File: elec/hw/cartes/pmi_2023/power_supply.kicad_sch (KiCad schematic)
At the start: 46 parts, among them J5 254, J8 254, Q3 DMP2008UFG-7, SW8 MSS12C02LS-BB2.0, U28 TLV61070A, U29 TLV61070A, U33 TLV61070A, U34 TLV61070A, U35 LDL1117S33R

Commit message: added oled display power supply res selectors, jlcpcb refs : wip
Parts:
- C27, C30, C39, C40: value 10µF 16V -> 10µF 25V; symbol cocotter_capacitors:C_10µF_16V_0805 -> cocotter_capacitors:C_10µF_25V_0805_X5R; JLCPCB (none) -> C15850; Specification 10µF 16V X7R 0805 -> 10µF 25V X7R 0805
- C29, C37, C41, C42: JLCPCB (none) -> C107079
- C46: symbol cocotter_capacitors:C_10µF_16V_0805_X5R -> cocotter_capacitors:C_10µF_25V_0805_X5R; Specification 10µF 25V X5R 0805 -> 10µF 25V X7R 0805
- D7: value red, 0603 -> white, 0603
- L1, L2, L3, L4: MOUSER (none) -> 581-LMLP07A7M2R2DTAS
- Q3: JLCPCB (none) -> C461052
- R107, R108, R111, R113: value 10k -> 10k 1%
- R110, R112, R67: value 90k -> 91k 1%; symbol cocotter_resistors:R_90k_0603_1% -> cocotter_resistors:R_91k_0603_1%; JLCPCB (none) -> C23265; Specification 90k 0603 1% 100mW -> 91k 0603 1% 100mW
- R66: JLCPCB (none) -> C23231
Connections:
- net GND: now also D7.1 (K); no longer D7.C
- net enable_pw_conv_3v7: now also D7.2 (A); no longer D7.A
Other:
- moved on the sheet: BT1

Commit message: reset button added to esp32 reset. uart prog connector replaces ftdi one
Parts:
- removed BT1: Battery_Cell, symbol Device:Battery_Cell
- added BT1: Battery 18650, symbol cocotter_others:Battery_Cell-18650
- D7: footprint cocotter_diodes:LED_0603_1608Metric -> (none)
- J5, J8: footprint cocotter_connectors:MY-18650-02 -> (none)

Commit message: pmi2023 : drc cleanup
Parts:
- D7: footprint (none) -> cocotter_diodes:LED_0603_1608Metric
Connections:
- net GND: now also D7.C; no longer D7.1 (C)
- net enable_pw_conv_3v7: now also D7.A; no longer D7.2 (A)
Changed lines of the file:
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@@
 			)
 		)
-		(property "Footprint" ""
+		(property "Footprint" "cocotter_diodes:LED_0603_1608Metric"
 			(at 82.55 62.23 0)
 			(effects
@@
 			)
 		)
-		(pin "1"
+		(pin "C"
 		)
-		(pin "2"
+		(pin "A"
 		)
 		(instances

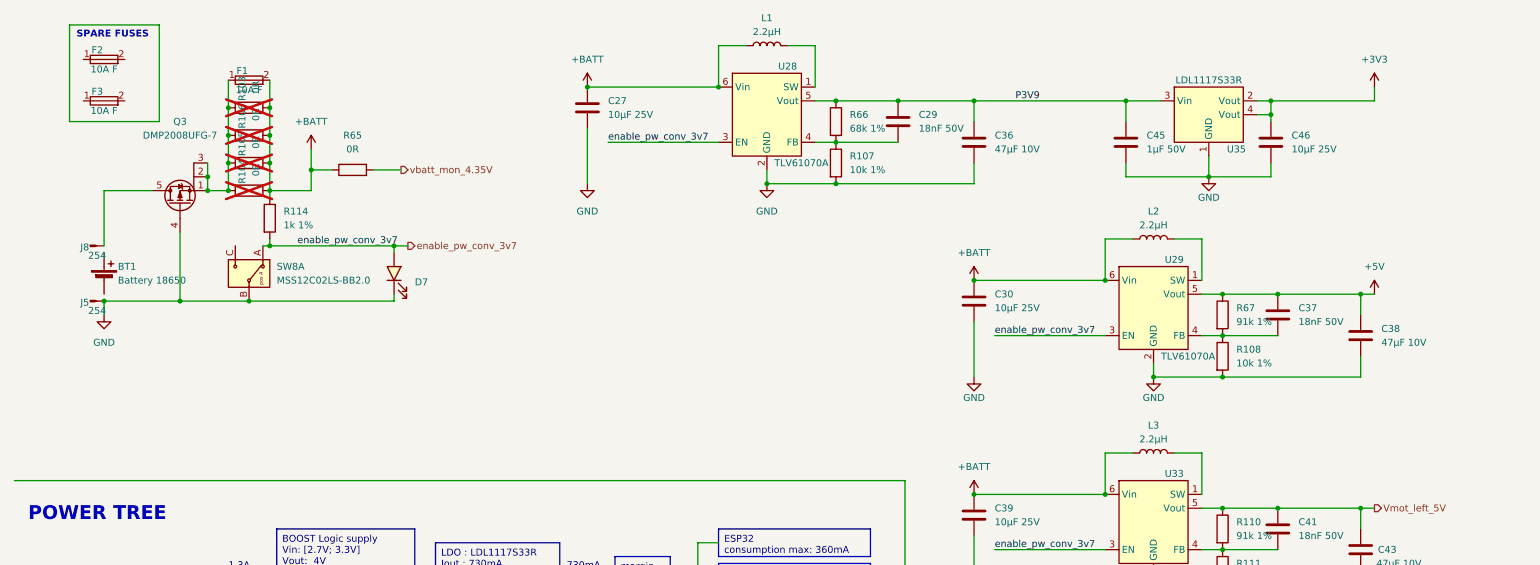
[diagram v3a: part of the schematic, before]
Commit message: routing cleanup, test points added to allow charging of battery in the pmi
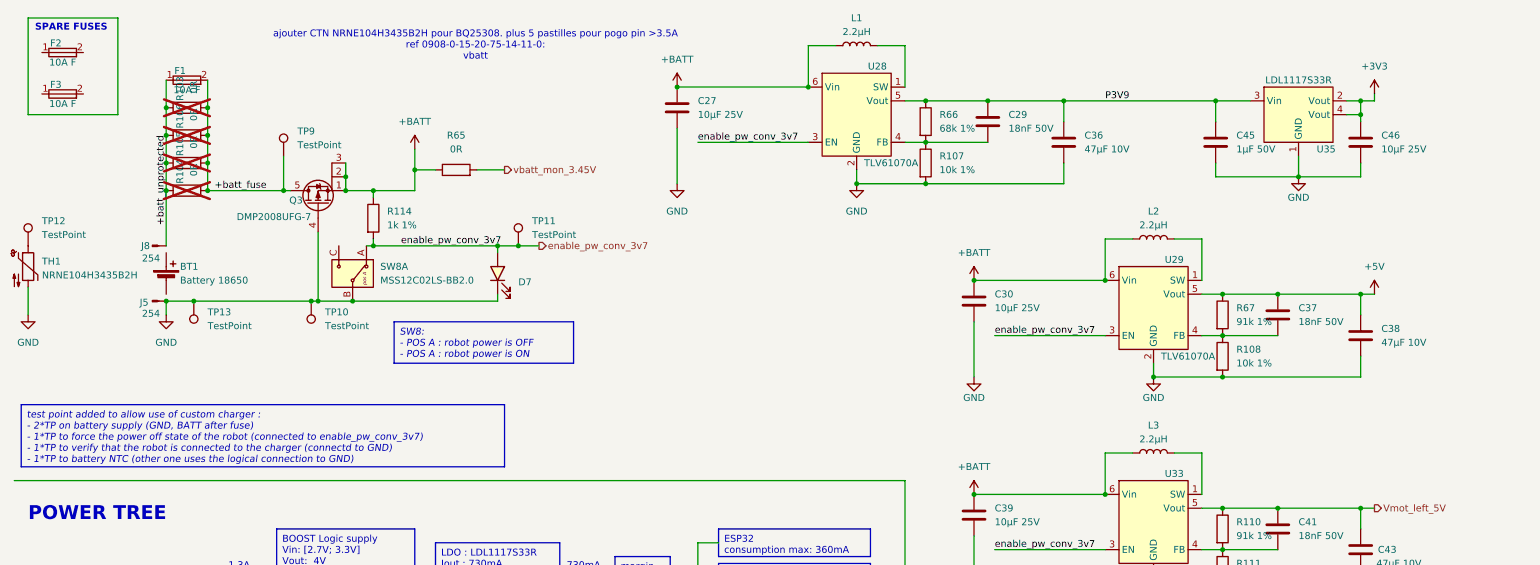
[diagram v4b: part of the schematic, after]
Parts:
- added TH1: NRNE104H3435B2H, cocotter_resistor:CTN-NRN, symbol cocotter_resistors:NRNE104H3435B2H
- added TP10, TP11, TP12, TP13, TP9: TestPoint, cocotter_others:testpoint-THT-0.5mm, symbol cocotter_others:TestPoint_for_pogo_pin-1mm
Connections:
- net +BATT: now also Q3.1 (S), Q3.2 (S), Q3.3 (S); no longer F1.2, R103.2, R104.2, R105.2, R106.2
- net GND: now also TH1.2, TP10.1, TP13.1
- net enable_pw_conv_3v7: now also TP11.1
- net +batt_unprotected: now reaches F1.1, R103.1, R104.1, R105.1, R106.1
- net +batt_unprotected: now also J8.1 (GND); no longer Q3.1 (S), Q3.2 (S), Q3.3 (S)
- net +batt_fuse: now reaches Q3.5 (D)
- net +batt_fuse: now also F1.2, R103.2, R104.2, R105.2, R106.2, TP9.1; no longer J8.1 (GND)
- net vbatt_mon_4.35V renamed vbatt_mon_3.45V
- new net: TH1.1, TP12.1
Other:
- note added: "ajouter CTN NRNE104H3435B2H pour BQ25308. plus 5 pastilles pour pogo pin >3.5A ref 0908-0-15-20-75-14-11-0: vbatt"
- moved on the sheet: BT1, C27, C29, C36, C45, C46, D7, F1, F2, F3, J5, J8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

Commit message: small changes
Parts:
- J5, J8: footprint (none) -> cocotter_connectors:254
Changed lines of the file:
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@@
 			)
 		)
-		(property "Footprint" ""
+		(property "Footprint" "cocotter_connectors:254"
 			(at 38.1 69.85 0)
 			(effects
@@
 			)
 		)
-		(property "Footprint" ""
+		(property "Footprint" "cocotter_connectors:254"
 			(at 38.1 59.69 0)
 			(effects

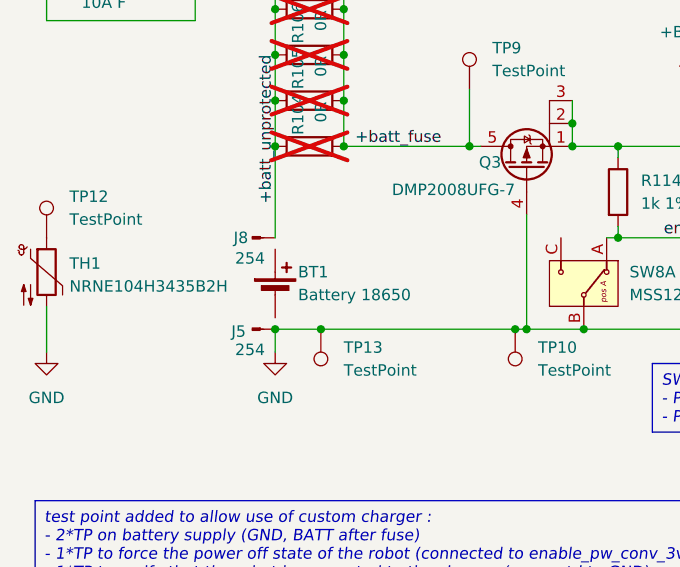
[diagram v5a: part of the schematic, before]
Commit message: PAMI 2023: update jlc part number
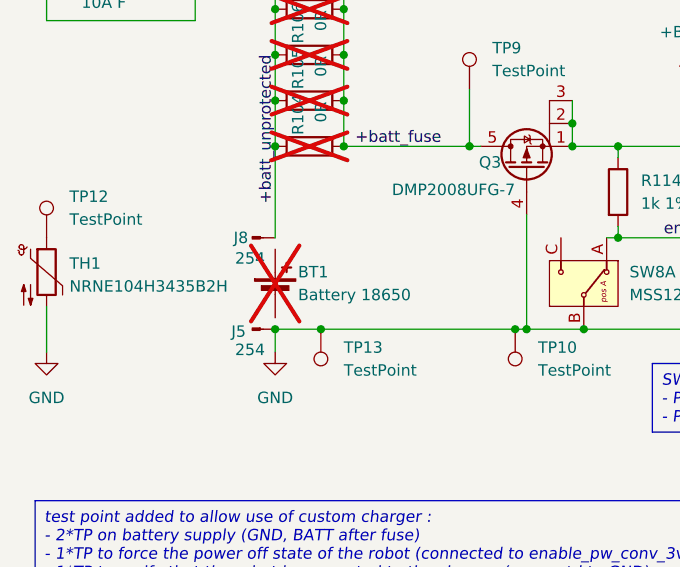
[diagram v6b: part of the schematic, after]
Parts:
- BT1: now not fitted
- L1, L2, L3, L4: JLCPCB (none) -> C1858011
- R114: JLCPCB C2991540 -> C21190
- U28, U29, U33, U34: JLCPCB (none) -> C6881375
- U35: JLCPCB (none) -> C435835
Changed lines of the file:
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@@
 			)
 		)
-		(property "JLCPCB" ""
+		(property "JLCPCB" "C1858011"
 			(at 222.25 95.25 0)
 			(effects
@@
 			)
 		)
-		(property "JLCPCB" ""
+		(property "JLCPCB" "C1858011"
 			(at 167.64 20.32 0)
 			(effects
@@
 			)
 		)
-		(property "JLCPCB" ""
+		(property "JLCPCB" "C1858011"
 			(at 222.25 134.62 0)
 			(effects
@@
 			)
 		)
+		(property "JLCPCB" "C435835"
+			(at 248.92 33.02 0)
+			(effects
+				(font
+					(size 1.27 1.27)
+				)
+				(hide yes)
+			)
+		)
 		(pin "3"
 		)
@@
 			)
 		)
-		(property "JLCPCB" ""
+		(property "JLCPCB" "C6881375"
 			(at 167.64 33.02 0)
 			(effects
@@
 			)
 		)
-		(property "JLCPCB" ""
+		(property "JLCPCB" "C6881375"
 			(at 222.25 147.32 0)
 			(effects
@@
 			)
 		)
-		(property "JLCPCB" ""
+		(property "JLCPCB" "C6881375"
 			(at 222.25 68.58 0)
 			(effects
@@
 		(in_bom no)
 		(on_board no)
-		(dnp no)
+		(dnp yes)
 		(property "Reference" "BT1"
 			(at 43.18 60.96 0)
@@
 			)
 		)
-		(property "JLCPCB" ""
+		(property "JLCPCB" "C6881375"
 			(at 222.25 107.95 0)
 			(effects
@@
 			)
 		)
-		(property "JLCPCB" "C2991540"
+		(property "JLCPCB" "C21190"
 			(at 78.74 52.07 0)
 			(effects
@@
 			)
 		)
-		(property "JLCPCB" ""
+		(property "JLCPCB" "C1858011"
 			(at 222.25 55.88 0)
 			(effects

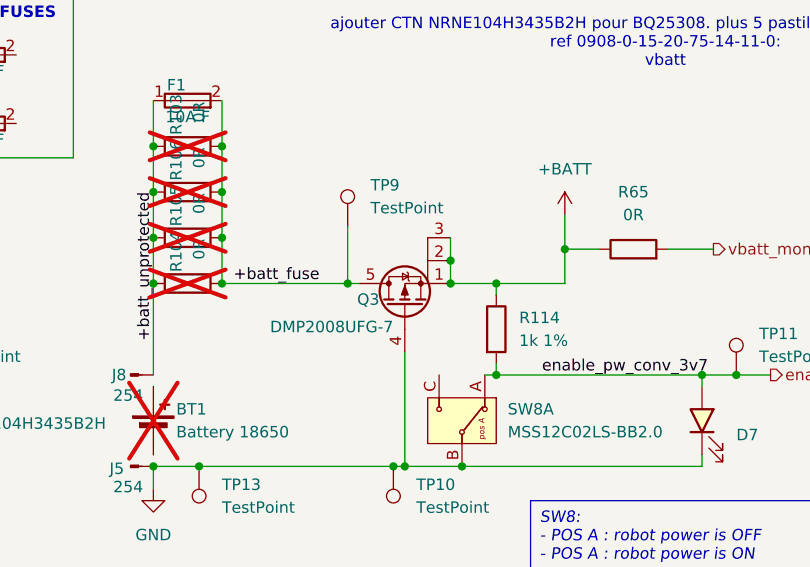
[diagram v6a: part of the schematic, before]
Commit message: XRA1200 replaced by TCA6408
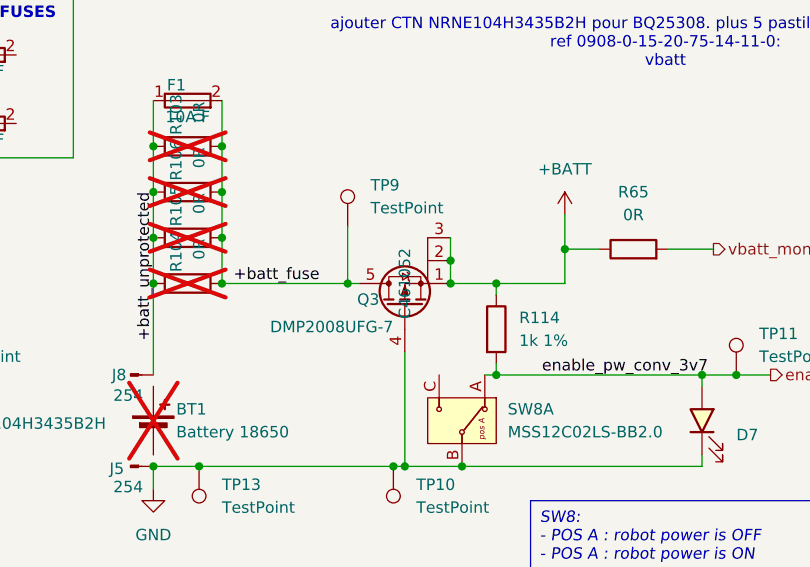
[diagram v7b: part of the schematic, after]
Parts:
- C27, C30, C39, C40, C46: JLCPCB C15850 -> (none); JLCPCB Part # (none) -> C15850
- C29, C37, C41, C42: JLCPCB C107079 -> (none); JLCPCB Part # (none) -> C107079
- C36, C38, C43, C44: JLCPCB C96123 -> (none); JLCPCB Part # (none) -> C96123
- C45: JLCPCB C28323 -> (none); JLCPCB Part # (none) -> C28323
- D7: JLCPCB C2290 -> (none); JLCPCB Part # (none) -> C2290
- F1, F2, F3: JLCPCB C136374 -> (none); JLCPCB Part # (none) -> C136374
- J5, J8: JLCPCB C2979182 -> (none); JLCPCB Part # (none) -> C2979182
- L1, L2, L3, L4: JLCPCB C1858011 -> (none); Mouser 581-LMLP07A7M2R2DTAS -> (none)
- Q3: JLCPCB C461052 -> (none); JLCPCB Part # (none) -> C461052
- R103, R104, R105, R106, R65: JLCPCB C431718 -> (none); JLCPCB Part # (none) -> C431718
- R107, R108, R111, R113: JLCPCB C25804 -> (none); JLCPCB Part # (none) -> C25804
- R110, R112, R67: JLCPCB C23265 -> (none); JLCPCB Part # (none) -> C23265
- R114: JLCPCB C21190 -> (none); JLCPCB Part # (none) -> C2991540
- R66: JLCPCB C23231 -> (none); JLCPCB Part # (none) -> C23231
- SW8: JLCPCB C3008585 -> (none); JLCPCB Part # (none) -> C3008585
- U28, U29, U33, U34: JLCPCB C6881375 -> (none)
- U35: JLCPCB C435835 -> (none)
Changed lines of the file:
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@@
 			)
 		)
-		(property "JLCPCB" "C136374"
+		(property "JLCPCB Part #" "C136374"
 			(at 44.45 29.21 0)
 			(effects
@@
 			)
 		)
-		(property "Mouser" "581-LMLP07A7M2R2DTAS"
-			(at 222.25 95.25 0)
-			(effects
-				(font
-					(size 1.27 1.27)
-				)
-				(justify right)
-				(hide yes)
-			)
-		)
-		(property "JLCPCB" "C1858011"
+		(property "MOUSER" "581-LMLP07A7M2R2DTAS"
 			(at 222.25 95.25 0)
 			(effects
@@
 			)
 		)
-		(property "MOUSER" "581-LMLP07A7M2R2DTAS"
+		(property "JLCPCB Part #" ""
 			(at 222.25 95.25 0)
 			(effects
@@
 			)
 		)
-		(property "JLCPCB" "C2290"
+		(property "JLCPCB Part #" "C2290"
 			(at 101.6 62.23 0)
 			(effects
@@
 			)
 		)
-		(property "JLCPCB" "C23265"
+		(property "JLCPCB Part #" "C23265"
 			(at 234.95 109.22 0)
 			(effects
@@
 			)
 		)
-		(property "JLCPCB" "C15850"
+		(property "JLCPCB Part #" "C15850"
 			(at 134.62 31.75 0)
 			(effects
@@
 			)
 		)
-		(property "JLCPCB" "C461052"
+		(property "JLCPCB Part #" "C461052"
 			(at 68.58 46.99 0)
 			(effects
@@
 					(size 1.27 1.27)
 				)
-				(hide yes)
 			)
 		)
@@
 			)
 		)
-		(property "JLCPCB" "C431718"
+		(property "JLCPCB Part #" "C431718"
 			(at 93.98 43.18 0)
 			(effects
@@
 			)
 		)
-		(property "JLCPCB" "C2979182"
+		(property "JLCPCB Part #" "C2979182"
 			(at 38.1 69.85 0)
 			(effects
@@
 			)
 		)
-		(property "JLCPCB" "C431718"
+		(property "JLCPCB Part #" "C431718"
 			(at 44.45 31.75 0)
 			(effects
@@
 			)
 		)
-		(property "JLCPCB" "C3008585"
+		(property "JLCPCB Part #" "C3008585"
 			(at 69.85 60.96 0)
 			(effects
@@
 			)
 		)
-		(property "JLCPCB" "C96123"
+		(property "JLCPCB Part #" "C96123"
 			(at 260.35 152.4 0)
 			(effects
@@
 			)
 		)
-		(property "JLCPCB" "C25804"
+		(property "JLCPCB Part #" "C25804"
 			(at 180.34 41.91 0)
 			(effects
@@
 			)
 		)
-		(property "JLCPCB" "C107079 "
+		(property "JLCPCB Part #" "C107079 "
 			(at 245.11 69.85 0)
 			(effects
@@
 			)
 		)
-		(property "Mouser" "581-LMLP07A7M2R2DTAS"
-			(at 167.64 20.32 0)
-			(effects
-				(font
-					(size 1.27 1.27)
-				)
-				(justify right)
-				(hide yes)
-			)
-		)
-		(property "JLCPCB" "C1858011"
+		(property "MOUSER" "581-LMLP07A7M2R2DTAS"
 			(at 167.64 20.32 0)
 			(effects
@@
 			)
 		)
-		(property "MOUSER" "581-LMLP07A7M2R2DTAS"
+		(property "JLCPCB Part #" ""
 			(at 167.64 20.32 0)
 			(effects
@@
 			)
 		)
-		(property "JLCPCB" "C25804"
+		(property "JLCPCB Part #" "C25804"
 			(at 234.95 156.21 0)
 			(effects
@@
 			)
 		)
-		(property "Mouser" "581-LMLP07A7M2R2DTAS"
-			(at 222.25 134.62 0)
-			(effects
-				(font
-					(size 1.27 1.27)
-				)
-				(justify right)
-				(hide yes)
-			)
-		)
-		(property "JLCPCB" "C1858011"
+		(property "MOUSER" "581-LMLP07A7M2R2DTAS"
 			(at 222.25 134.62 0)
 			(effects
@@
 			)
 		)
-		(property "MOUSER" "581-LMLP07A7M2R2DTAS"
+		(property "JLCPCB Part #" ""
 			(at 222.25 134.62 0)
 			(effects
@@
 			)
 		)
-		(property "JLCPCB" "C107079 "
+		(property "JLCPCB Part #" "C107079 "
 			(at 245.11 148.59 0)
 			(effects
@@
 			)
 		)
-		(property "JLCPCB" "C15850"
+		(property "JLCPCB Part #" "C15850"
 			(at 189.23 106.68 0)
 			(effects
@@
 			)
 		)
-		(property "JLCPCB" "C435835"
-			(at 248.92 33.02 0)
-			(effects
-				(font
-					(size 1.27 1.27)
-				)
-				(hide yes)
-			)
-		)
 		(pin "3"
 		)
@@
 			)
 		)
-		(property "JLCPCB" "C136374"
+		(property "JLCPCB Part #" "C136374"
 			(at 21.59 24.13 0)
 			(effects
@@
 			)
 		)
-		(property "JLCPCB" "C96123"
+		(property "JLCPCB Part #" "C96123"
 			(at 205.74 38.1 0)
 			(effects
@@
 			)
 		)
-		(property "JLCPCB" "C23231"
+		(property "JLCPCB Part #" "C23231"
 			(at 180.34 34.29 0)
 			(effects
@@
 			)
 		)
-		(property "JLCPCB" "C23265"
+		(property "JLCPCB Part #" "C23265"
 			(at 234.95 69.85 0)
 			(effects
@@
 			)
 		)
-		(property "JLCPCB" "C107079 "
+		(property "JLCPCB Part #" "C107079 "
 			(at 245.11 109.22 0)
 			(effects
@@
 			)
 		)
-		(property "JLCPCB" "C96123"
+		(property "JLCPCB Part #" "C96123"
 			(at 260.35 73.66 0)
 			(effects
@@
 			)
 		)
-		(property "JLCPCB" "C6881375"
+		(property "JLCPCB Part #" ""
 			(at 167.64 33.02 0)
 			(effects
@@
 			)
 		)
-		(property "JLCPCB" "C6881375"
+		(property "JLCPCB Part #" ""
 			(at 222.25 147.32 0)
 			(effects
@@
 			)
 		)
-		(property "JLCPCB" "C25804"
+		(property "JLCPCB Part #" "C25804"
 			(at 234.95 77.47 0)
 			(effects
@@
 			)
 		)
-		(property "JLCPCB" "C6881375"
+		(property "JLCPCB Part #" ""
 			(at 222.25 68.58 0)
 			(effects
@@
 			)
 		)
-		(property "JLCPCB" "C15850"
+		(property "JLCPCB Part #" "C15850"
 			(at 189.23 67.31 0)
 			(effects
@@
 			)
 		)
-		(property "JLCPCB" "C107079 "
+		(property "JLCPCB Part #" "C107079 "
 			(at 191.77 34.29 0)
 			(effects
@@
 			)
 		)
-		(property "JLCPCB" "C15850"
+		(property "JLCPCB Part #" "C15850"
 			(at 260.35 38.1 0)
 			(effects
@@
 			)
 		)
-		(property "JLCPCB" "C25804"
+		(property "JLCPCB Part #" "C25804"
 			(at 234.95 116.84 0)
 			(effects
@@
 			)
 		)
-		(property "JLCPCB" "C28323"
+		(property "JLCPCB Part #" "C28323"
 			(at 233.68 38.1 0)
 			(effects
@@
 			)
 		)
-		(property "JLCPCB" "C2979182"
+		(property "JLCPCB Part #" "C2979182"
 			(at 38.1 59.69 0)
 			(effects
@@
 			)
 		)
-		(property "JLCPCB" "C96123"
+		(property "JLCPCB Part #" "C96123"
 			(at 260.35 113.03 0)
 			(effects
@@
 			)
 		)
-		(property "JLCPCB" "C15850"
+		(property "JLCPCB Part #" "C15850"
 			(at 189.23 146.05 0)
 			(effects
@@
 			)
 		)
-		(property "JLCPCB" "C431718"
+		(property "JLCPCB Part #" "C431718"
 			(at 44.45 46.99 0)
 			(effects
@@
 			)
 		)
-		(property "JLCPCB" "C23265"
+		(property "JLCPCB Part #" "C23265"
 			(at 234.95 148.59 0)
 			(effects
@@
 			)
 		)
-		(property "JLCPCB" "C136374"
+		(property "JLCPCB Part #" "C136374"
 			(at 21.59 31.75 0)
 			(effects
@@
 			)
 		)
-		(property "JLCPCB" "C431718"
+		(property "JLCPCB Part #" "C431718"
 			(at 44.45 36.83 0)
 			(effects
@@
 			)
 		)
-		(property "JLCPCB" "C6881375"
+		(property "JLCPCB Part #" ""
 			(at 222.25 107.95 0)
 			(effects
@@
 			)
 		)
-		(property "JLCPCB" "C431718"
+		(property "JLCPCB Part #" "C431718"
 			(at 44.45 41.91 0)
 			(effects
@@
 			)
 		)
-		(property "JLCPCB" "C21190"
+		(property "JLCPCB Part #" "C2991540"
 			(at 78.74 52.07 0)
 			(effects
@@
 			)
 		)
-		(property "Mouser" "581-LMLP07A7M2R2DTAS"
-			(at 222.25 55.88 0)
-			(effects
-				(font
-					(size 1.27 1.27)
-				)
-				(justify right)
-				(hide yes)
-			)
-		)
-		(property "JLCPCB" "C1858011"
+		(property "MOUSER" "581-LMLP07A7M2R2DTAS"
 			(at 222.25 55.88 0)
 			(effects
@@
 			)
 		)
-		(property "MOUSER" "581-LMLP07A7M2R2DTAS"
+		(property "JLCPCB Part #" ""
 			(at 222.25 55.88 0)
 			(effects
